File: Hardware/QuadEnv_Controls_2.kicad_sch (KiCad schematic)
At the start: 14 parts, among them J1 Conn_01x04_Male, J2 Conn_01x05_Male, J3 Conn_01x04_Male, J4 Conn_01x04_Male, J5 Gate_In, J6 Env_Out

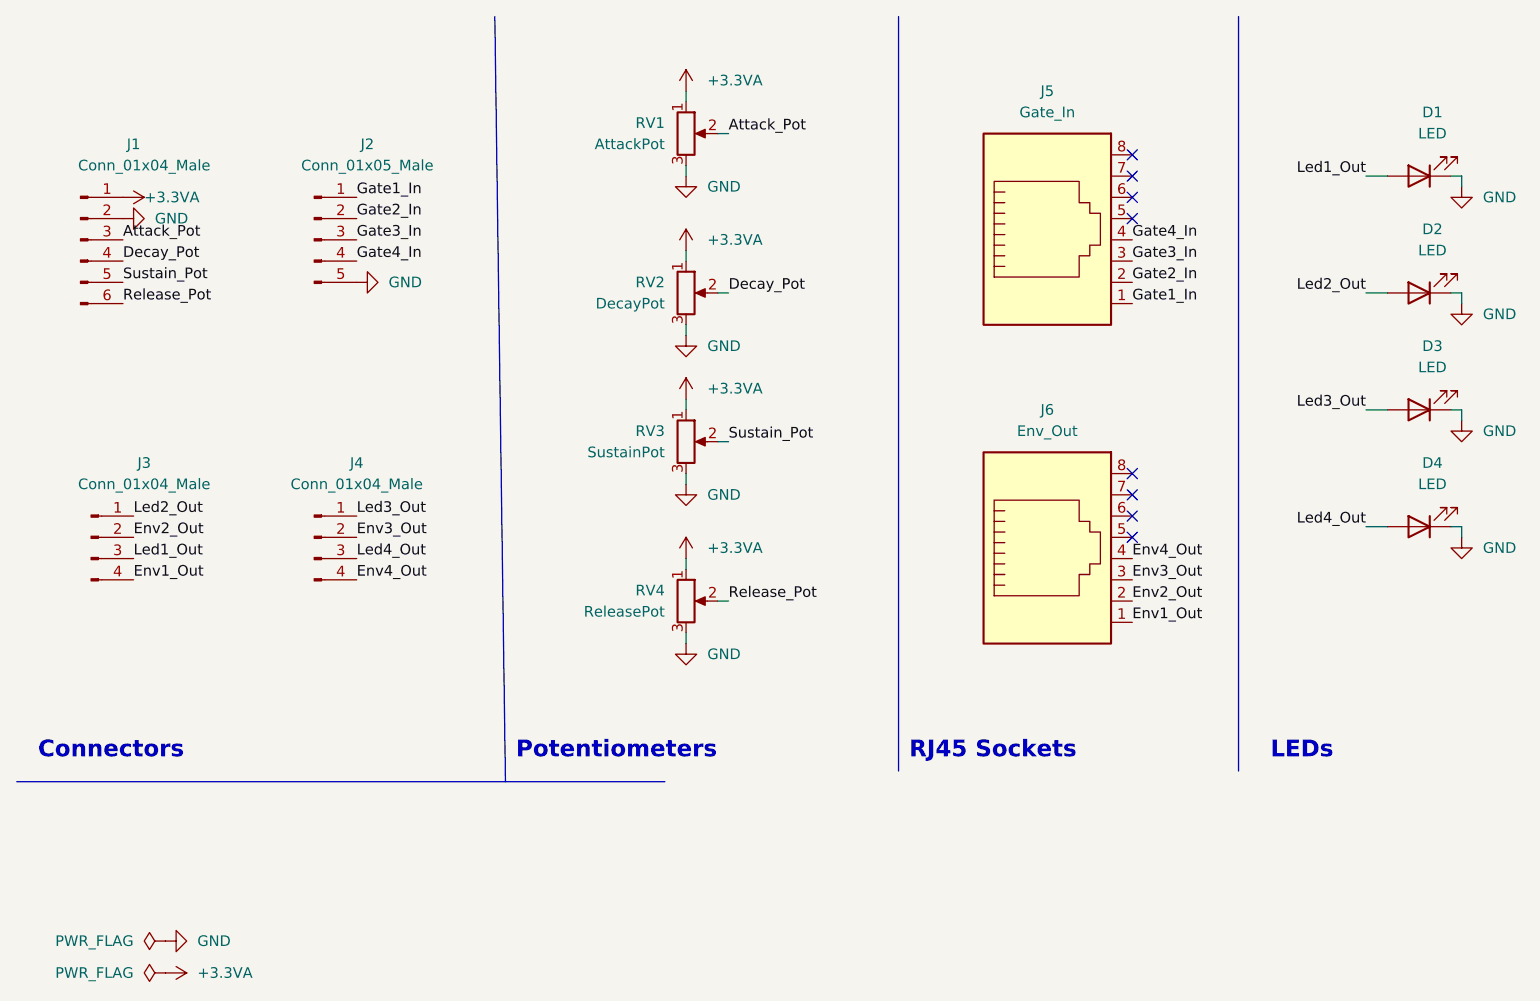
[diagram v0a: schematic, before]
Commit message: Updated components and controls to include mode button/led
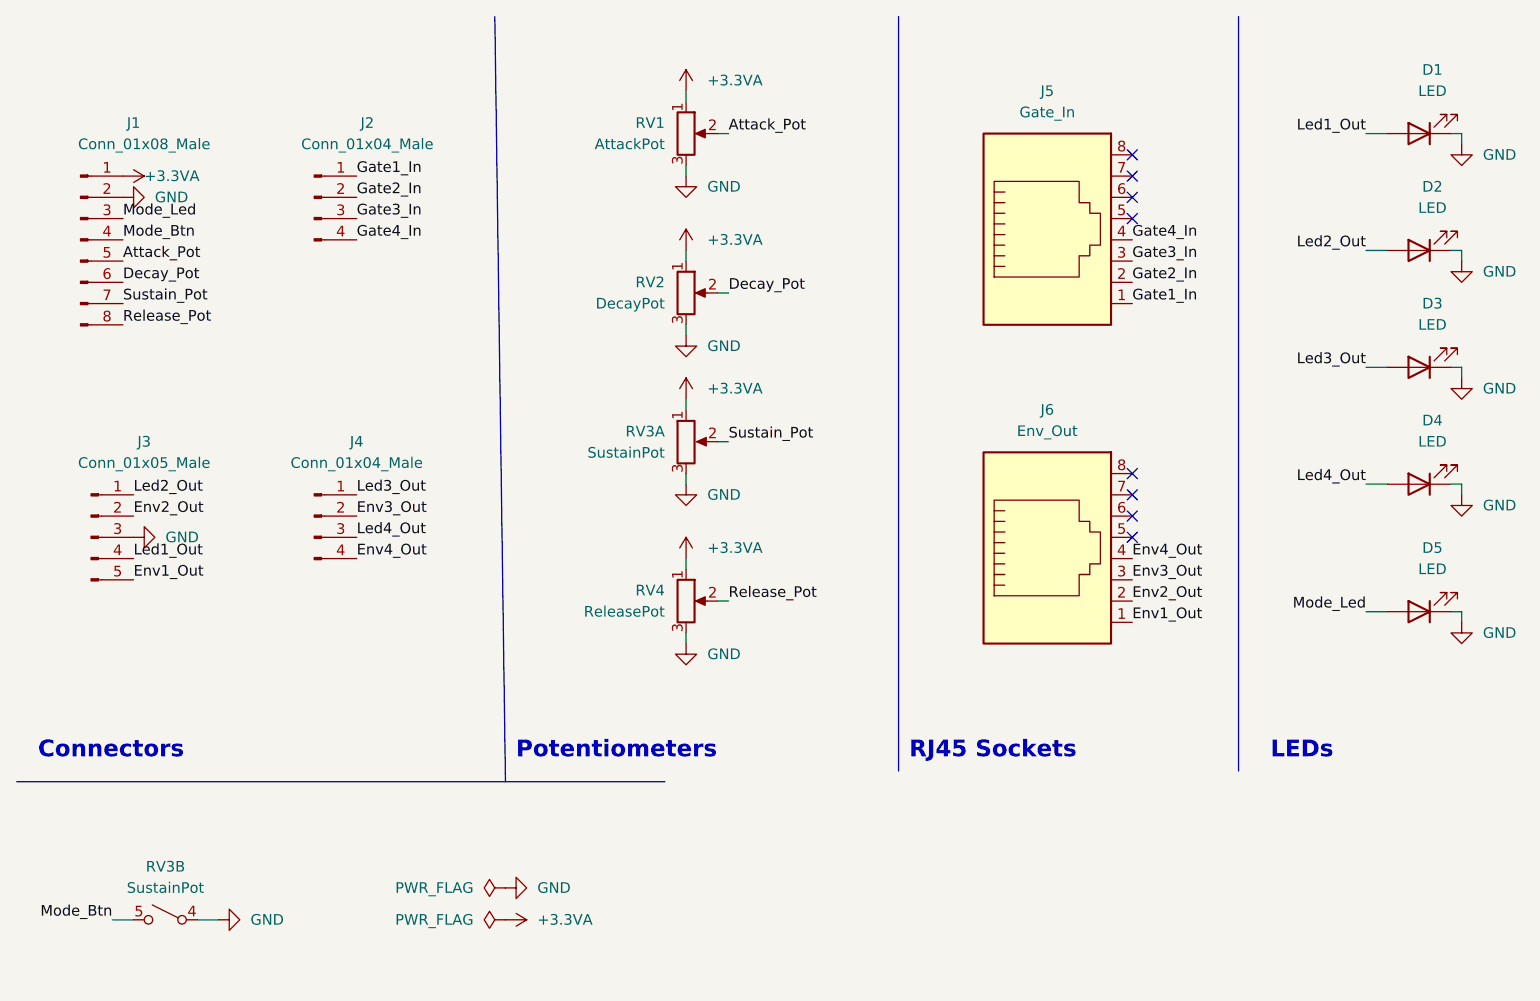
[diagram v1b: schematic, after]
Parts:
- removed RV3: SustainPot, Custom_Footprints:Alpha_9mm_Potentiometer_Aligned, symbol Device:R_Potentiometer
- added D5: LED, Custom_Footprints:LED_D3.0mm, symbol Device:LED
- added RV3: SustainPot, Custom_Footprints:Bourns_Switch_Potentiometer, symbol Mountjoy:Switch_Potentiometer
- J1: value Conn_01x04_Male -> Conn_01x08_Male; footprint Connector_PinHeader_2.54mm:PinHeader_1x06_P2.54mm_Vertical -> Connector_PinHeader_2.54mm:PinHeader_1x08_P2.54mm_Vertical; symbol Connector:Conn_01x06_Male -> Connector:Conn_01x08_Pin
- J2: value Conn_01x05_Male -> Conn_01x04_Male; footprint Connector_PinHeader_2.54mm:PinHeader_1x05_P2.54mm_Vertical -> Connector_PinHeader_2.54mm:PinHeader_1x04_P2.54mm_Vertical; symbol Connector:Conn_01x05_Male -> Connector:Conn_01x04_Pin
- J3: value Conn_01x04_Male -> Conn_01x05_Male; footprint Connector_PinHeader_2.54mm:PinHeader_1x04_P2.54mm_Vertical -> Connector_PinHeader_2.54mm:PinHeader_1x05_P2.54mm_Vertical; symbol Connector:Conn_01x04_Male -> Connector:Conn_01x05_Pin
- J4: symbol Connector:Conn_01x04_Male -> Connector:Conn_01x04_Pin
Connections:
- net +3.3VA: now also RV3.1
- net Attack_Pot: now also J1.5 (Pin_5); no longer J1.3 (Pin_3)
- net Decay_Pot: now also J1.6 (Pin_6); no longer J1.4 (Pin_4)
- net Env1_Out: now also J3.5 (Pin_5); no longer J3.4 (Pin_4)
- net GND: now also J3.3 (Pin_3), D5.1 (K), RV3.3, RV3.4 (1); no longer J2.5 (Pin_5)
- net Led1_Out: now also J3.4 (Pin_4); no longer J3.3 (Pin_3)
- net Release_Pot: now also J1.8 (Pin_8); no longer J1.6 (Pin_6)
- net Sustain_Pot: now also J1.7 (Pin_7), RV3.2; no longer J1.5 (Pin_5)
- new net Mode_Btn: J1.4 (Pin_4), RV3.5 (2)
- new net Mode_Led: D5.2 (A), J1.3 (Pin_3)
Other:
- moved on the sheet: D1, D2, D3, D4, J4

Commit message: Updated to version 2 of panel
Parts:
- J1: value Conn_01x08_Male -> Conn_01x08; footprint Connector_PinHeader_2.54mm:PinHeader_1x08_P2.54mm_Vertical -> Connector_PinSocket_2.54mm:PinSocket_1x08_P2.54mm_Vertical; symbol Connector:Conn_01x08_Pin -> Connector:Conn_01x08_Socket
- J2, J4: value Conn_01x04_Male -> Conn_01x04; footprint Connector_PinHeader_2.54mm:PinHeader_1x04_P2.54mm_Vertical -> Connector_PinSocket_2.54mm:PinSocket_1x04_P2.54mm_Vertical; symbol Connector:Conn_01x04_Pin -> Connector:Conn_01x04_Socket
- J3: value Conn_01x05_Male -> Conn_01x05; footprint Connector_PinHeader_2.54mm:PinHeader_1x05_P2.54mm_Vertical -> Connector_PinSocket_2.54mm:PinSocket_1x05_P2.54mm_Vertical; symbol Connector:Conn_01x05_Pin -> Connector:Conn_01x05_Socket
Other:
- moved on the sheet: J5, J6, RV3B
